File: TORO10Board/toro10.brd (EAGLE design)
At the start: 100 x 100 mm, 358 parts, among them CN1 5569-04A2, CN10 ALTERA-JTAG-TH1.27, CN11 53426-0410, CN12 43045-0800, CN13 53426-0410, CN14 43045-0800, CN15 53426-0410, CN16 43045-0800, CN17 53426-0410, CN18 43045-0800, CN19 53426-0410, CN2 3557-20, CN20 PIN1X8, CN3 43045-0800, CN4 PIN1X2, CN5 PIN1X2, CN6 SOCKET1X10, CN7 SOCKET1X10, CN8 External, CN9 ALTERA-JTAG-TH2.54, J1 JUMPER1X3, J2 JUMPER2X5, Q1 BSS138, Q10 BSS138, Q11 BSS138, Q12 BSS138, Q2 2SC2712, Q3 BSS138, Q4 BSS138, Q5 BSS138, Q6 2SC2712, Q7 SI7135DP, Q8 TPN7R506NH, Q9 TPN7R506NH, SW1 B-12JV, SW2 EVQ-PUB02K, SW3 EVQ-PUB02K, U1 INA219, U10 SPX3819M5-L-5-0, U11 SN74LV165APW, U12 SN74LV165APW, U13 DRV8332, U14 INA240A2, U15 INA240A2, U16 DRV8332, U17 INA240A2, U18 INA240A2, U19 DRV8332, U2 LT3504, U20 INA240A2, U21 INA240A2, U22 DRV8332, U23 INA240A2, U24 INA240A2, U25 DRV8312, U3 LTC3862UH-1, U4 10M16SCE144, U5 IS25LP016D, U6 PCAL6416AHF, U7 24AA02E48, U8 ICM-20689, U9 ADS7223, X1 ASDMB-30.000MHZ-LC-T

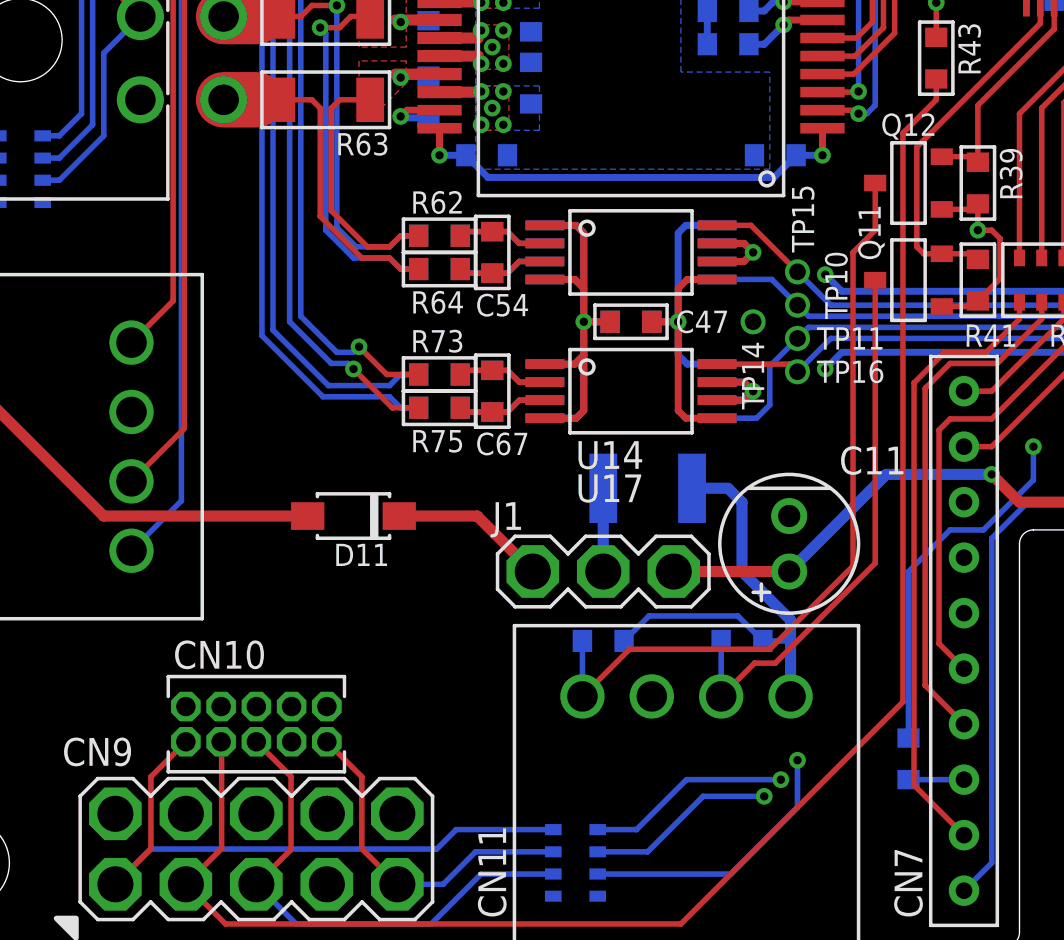
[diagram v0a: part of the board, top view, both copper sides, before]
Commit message: add kicker board
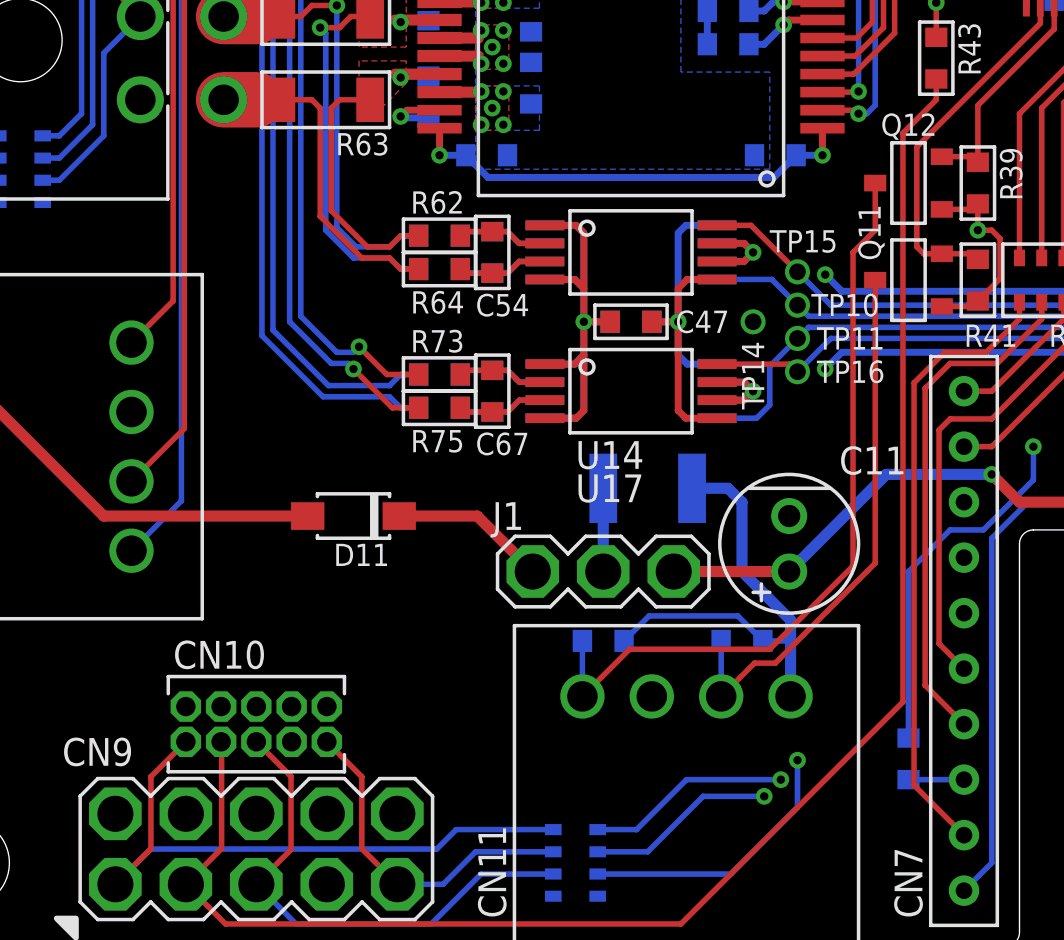
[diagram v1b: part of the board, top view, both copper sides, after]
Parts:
- CN10: device kiks-connector:PIN2X5-TH1.27 -> kiks-connector:PIN2X5-1.27
- CN4, CN5: value PIN1X2 -> (none)
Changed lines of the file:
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@@
 <attribute name="VALUE" x="0.9" y="65.7" size="0.8" layer="28" font="vector" ratio="18" rot="MR90"/>
 </element>
-<element name="CN5" library="kiks-connector" package="PIN1X2" value="PIN1X2" x="81.5" y="89.19" smashed="yes" rot="R270">
+<element name="CN5" library="kiks-connector" package="PIN1X2" value="" x="81.5" y="89.19" smashed="yes" rot="R270">
 <attribute name="NAME" x="83.01" y="87" size="1" layer="25" font="vector" ratio="15"/>
 <attribute name="VALUE" x="79" y="91.69" size="1" layer="27" font="vector" ratio="15" rot="R270"/>
@@
 <attribute name="VALUE" x="-0.1" y="95" size="1" layer="28" font="vector" ratio="15" rot="MR180"/>
 </element>
-<element name="CN4" library="kiks-connector" package="PIN1X2" value="PIN1X2" x="81.5" y="96.81" smashed="yes" rot="R270">
+<element name="CN4" library="kiks-connector" package="PIN1X2" value="" x="81.5" y="96.81" smashed="yes" rot="R270">
 <attribute name="NAME" x="81.59" y="93" size="1" layer="25" font="vector" ratio="15" align="bottom-center"/>
 <attribute name="VALUE" x="79" y="99.31" size="1" layer="27" font="vector" ratio="15" rot="R270"/>
@@
 <element name="TP2" library="kiks-mechanical" package="TESTPAD-TH" value="" x="65.5" y="74.9"/>
 <element name="TP15" library="kiks-mechanical" package="TESTPAD-TH" value="" x="33" y="24.3" smashed="yes">
-<attribute name="NAME" x="33.6" y="25" size="0.8" layer="25" font="vector" ratio="18" rot="R90"/>
+<attribute name="NAME" x="32" y="25" size="0.8" layer="25" font="vector" ratio="18"/>
 </element>
 <element name="TP16" library="kiks-mechanical" package="TESTPAD-TH" value="" x="33" y="20.7"/>
@@
 </element>
 <element name="TP10" library="kiks-mechanical" package="TESTPAD-TH" value="" x="33" y="23.1" smashed="yes">
-<attribute name="NAME" x="34.8" y="22.6" size="0.8" layer="25" font="vector" ratio="18" rot="R90"/>
+<attribute name="NAME" x="33.5" y="22.7" size="0.8" layer="25" font="vector" ratio="18"/>
 </element>
 <element name="TP11" library="kiks-mechanical" package="TESTPAD-TH" value="" x="33" y="21.9"/>
@@
 <element name="TP9" library="kiks-mechanical" package="TESTPAD-SMT" value="" x="1" y="73" rot="MR90"/>
 <element name="R33" library="kiks-passive" package="1608" value="2.2k" x="65" y="10.75" rot="R270"/>
-<element name="CN10" library="kiks-connector" package="PIN2X5-TH1.27" value="ALTERA-JTAG-TH1.27" x="13.5" y="8"/>
+<element name="CN10" library="kiks-connector" package="PIN2X5-1.27" value="ALTERA-JTAG-TH1.27" x="13.5" y="8"/>
 </elements>
 <signals>
